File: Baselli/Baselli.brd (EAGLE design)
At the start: 54 x 54 mm, 80 parts, among them J1 FTDI-SER-6-PP, J2 DF12-ELLI-HEADER-TOP, J3 DF12-ELLI-RECEPTABLE-BOTTOM, J4 JTAG_PROG, Q1 8MHz NP, Q2 IRLML2244, SW1 A6H-2101, U1 STM32F051R, U4 LCMXO2-256HC-4SG32, X1 M-BOLT-2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

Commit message: Baselli: Ripof all trials, move components as learned in the lesson
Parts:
- moved X2 50.2 mm to (5.50, 13.5)
- moved X3 50.2 mm to (48.5, 40.5)
- moved R5 28.1 mm to (14.0, 19.0)
- moved R10 23.2 mm to (20.0, 24.0)
- moved R11 19.1 mm to (14.0, 24.0)
- moved R12 16.3 mm to (20.0, 27.0)
- moved U4 15.7 mm to (41.0, 15.0)
- moved R13 12.2 mm to (14.0, 27.0)
- moved R14 9.49 mm to (20.0, 30.0)
- moved Q2 9.22 mm to (18.4, 11.8)
- moved R22 9.00 mm to (16.6, 8.89)
- moved D5 6.71 mm to (42.0, 41.0), turned to 270 degrees
- moved R20 6.71 mm to (24.0, 38.0)
- moved R18 5.83 mm to (20.0, 36.0)
- moved R15 5.39 mm to (14.0, 30.0)
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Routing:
- net +5V: track 58.2 -> 0.00 mm
- net +3V3: track 43.3 -> 0.00 mm
- net GNDI: track 41.9 -> 0.00 mm
- net VCCIO: track 21.5 -> 0.00 mm
- net NRES: track 14.3 -> 0.00 mm
- net DOUT: track 12.5 -> 0.00 mm
- net SWCLK: track 10.6 -> 0.00 mm
- net BOOT0TX: track 9.90 -> 0.00 mm
- net JTAGEN_GATE: track 9.00 -> 0.00 mm
- net -RTS: track 8.73 -> 0.00 mm
- net E12: track 5.88 -> 0.00 mm
- net E0: track 5.39 -> 0.00 mm
- net D4: track 5.05 -> 0.00 mm
- net VCC-IN: track 3.96 -> 0.00 mm
- net N$6: track 3.21 -> 0.00 mm
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
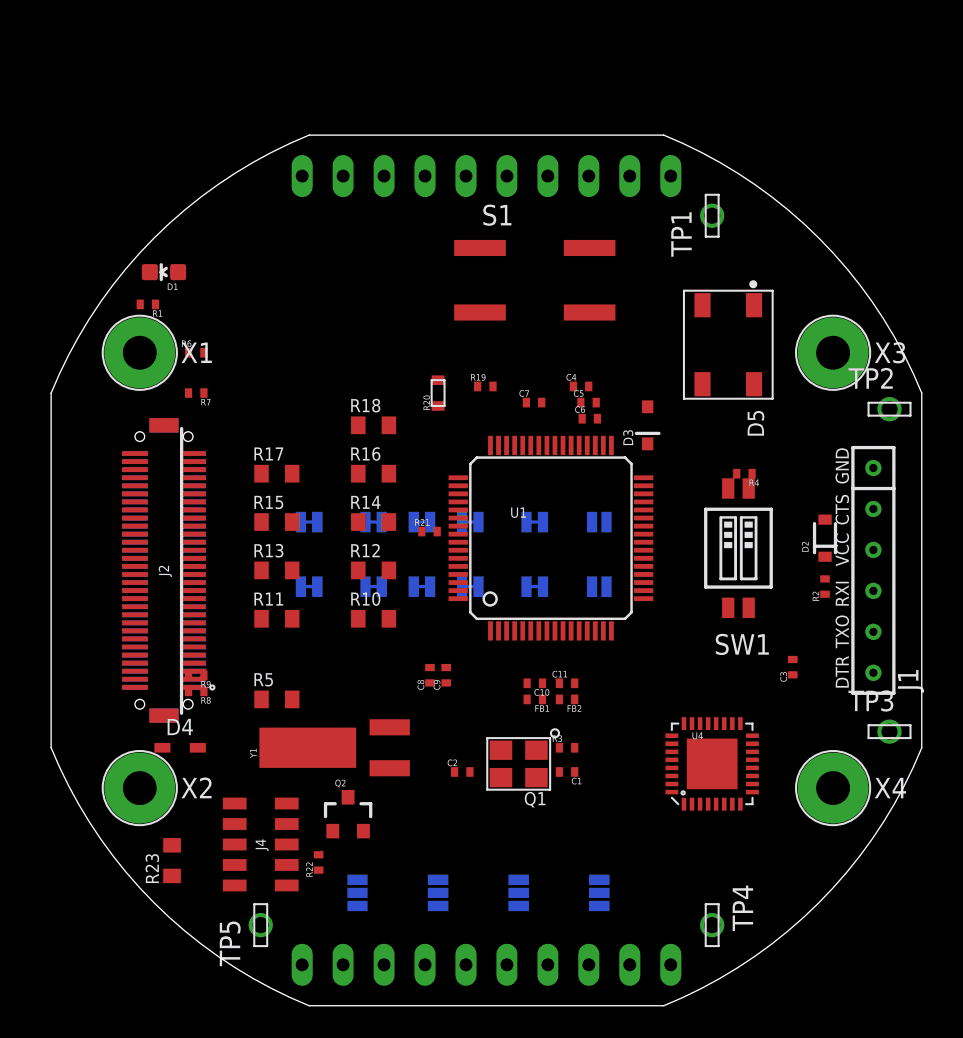
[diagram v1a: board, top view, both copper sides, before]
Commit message: Changes to Baselli from today's meeting
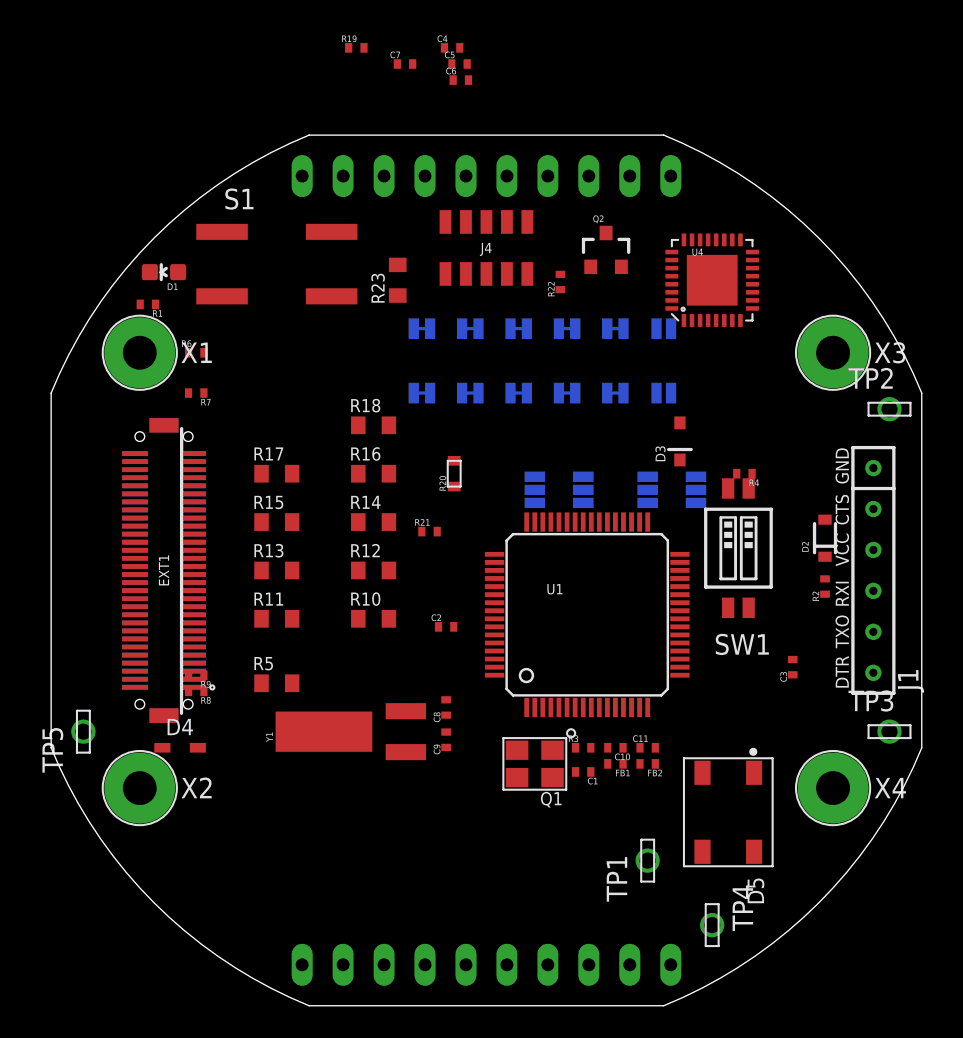
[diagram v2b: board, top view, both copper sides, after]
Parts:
- moved TP1 40.2 mm to (37.0, 9.00)
- moved J4 39.6 mm to (27.0, 47.0), turned to 0 degrees
- moved R22 39.0 mm to (31.6, 44.9)
- moved R23 38.6 mm to (21.5, 45.0)
- moved Q2 38.5 mm to (34.4, 46.8)
- moved U4 30.0 mm to (41.0, 45.0)
- moved D5 29.0 mm to (42.0, 12.0)
- moved SJ1 27.3 mm to (30.0, 32.0)
- moved SJ2 26.6 mm to (33.0, 32.0)
- moved SJ3 26.2 mm to (37.0, 32.0)
- moved SJ4 25.7 mm to (40.0, 32.0)
- moved C4 22.5 mm to (24.9, 59.4)
- moved C5 22.5 mm to (25.3, 58.4)
- moved C6 22.5 mm to (25.4, 57.4)
- moved C7 22.5 mm to (21.9, 58.4)
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- renumbered J2 to EXT1, J3 to EXB1
